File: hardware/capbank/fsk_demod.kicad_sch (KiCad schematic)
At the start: 13 parts, among them U10 TS861IL, U7 4046

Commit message: KiCad changes
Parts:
- removed R16: 10k, PCM_Resistor_SMD_AKL:R_0603_1608Metric, symbol Device:R
- added JP5, JP6: 0, PCM_Resistor_SMD_AKL:R_0603_1608Metric, symbol Jumper:Jumper_2_Small_Open
- C40, C41: value C -> 1n
- R13: value 10k -> 22k
- R14: now not fitted
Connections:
- net at C41.1: now also R15.2, U7.9 (VCOin)
- net at U7.2 (PC1): now also JP6.1 (A); no longer R15.1
- net at U7.13 (PC2): now also JP5.1 (A)
- new net: JP5.2 (B), JP6.2 (B), R15.1
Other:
- moved on the sheet: C41, R15
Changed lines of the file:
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@@
+	)
+	(junction
+		(at 87.63 113.03)
+		(diameter 0)
+		(color 0 0 0 0)
 	)
 	(junction
@@
 	(wire
 		(pts
+			(xy 85.09 115.57) (xy 87.63 115.57)
+		)
+		(stroke
+			(width 0)
+			(type default)
+		)
+	)
+	(wire
+		(pts
 			(xy 52.07 92.71) (xy 52.07 110.49)
 		)
@@
 	(wire
 		(pts
-			(xy 102.87 113.03) (xy 105.41 113.03)
+			(xy 100.33 113.03) (xy 105.41 113.03)
 		)
 		(stroke
@@
 	(wire
 		(pts
-			(xy 80.01 113.03) (xy 95.25 113.03)
-		)
-		(stroke
-			(width 0)
-			(type default)
-		)
-	)
-	(wire
-		(pts
-			(xy 114.3 132.08) (xy 114.3 140.97)
+			(xy 114.3 123.19) (xy 114.3 133.35)
 		)
 		(stroke
@@
 	(wire
 		(pts
+			(xy 87.63 113.03) (xy 87.63 115.57)
+		)
+		(stroke
+			(width 0)
+			(type default)
+		)
+	)
+	(wire
+		(pts
 			(xy 82.55 110.49) (xy 82.55 92.71)
 		)
@@
 	(wire
 		(pts
+			(xy 85.09 113.03) (xy 87.63 113.03)
+		)
+		(stroke
+			(width 0)
+			(type default)
+		)
+	)
+	(wire
+		(pts
 			(xy 105.41 113.03) (xy 105.41 120.65)
 		)
@@
 	(wire
 		(pts
-			(xy 114.3 123.19) (xy 114.3 124.46)
+			(xy 87.63 113.03) (xy 92.71 113.03)
 		)
 		(stroke
@@
 	(symbol
 		(lib_id "Device:C")
-		(at 114.3 128.27 0)
+		(at 114.3 119.38 0)
 		(unit 1)
 		(exclude_from_sim no)
@@
 		(fields_autoplaced yes)
 		(property "Reference" "C41"
-			(at 118.11 126.9999 0)
+			(at 118.11 118.1099 0)
 			(effects
 				(font
@@
 			)
 		)
-		(property "Value" "C"
-			(at 118.11 129.5399 0)
+		(property "Value" "1n"
+			(at 118.11 120.6499 0)
 			(effects
 				(font
@@
 		)
 		(property "Footprint" "PCM_Capacitor_SMD_AKL:C_0603_1608Metric"
-			(at 115.2652 132.08 0)
+			(at 115.2652 123.19 0)
 			(effects
 				(font
@@
 		)
 		(property "Datasheet" "~"
-			(at 114.3 128.27 0)
+			(at 114.3 119.38 0)
 			(effects
 				(font
@@
 		)
 		(property "Description" "Unpolarized capacitor"
-			(at 114.3 128.27 0)
+			(at 114.3 119.38 0)
 			(effects
 				(font
@@
 	)
 	(symbol
-		(lib_id "Device:R")
-		(at 114.3 119.38 0)
-		(unit 1)
-		(exclude_from_sim no)
-		(in_bom yes)
-		(on_board yes)
-		(dnp no)
-		(fields_autoplaced yes)
-		(property "Reference" "R16"
-			(at 116.84 118.1099 0)
-			(effects
-				(font
-					(size 1.27 1.27)
-				)
-				(justify left)
-			)
-		)
-		(property "Value" "10k"
-			(at 116.84 120.6499 0)
-			(effects
-				(font
-					(size 1.27 1.27)
-				)
-				(justify left)
-			)
-		)
-		(property "Footprint" "PCM_Resistor_SMD_AKL:R_0603_1608Metric"
-			(at 112.522 119.38 90)
-			(effects
-				(font
-					(size 1.27 1.27)
-				)
-				(hide yes)
-			)
-		)
-		(property "Datasheet" "~"
-			(at 114.3 119.38 0)
-			(effects
-				(font
-					(size 1.27 1.27)
-				)
-				(hide yes)
-			)
-		)
-		(property "Description" "Resistor"
-			(at 114.3 119.38 0)
-			(effects
-				(font
-					(size 1.27 1.27)
-				)
-				(hide yes)
-			)
-		)
-		(pin "2"
-		)
-		(pin "1"
-		)
-		(instances
-			(project "capbank1"
-				(path "/461cb8a1-2d60-44a8-88b5-d61a3ba14a84/d9c36704-5831-4033-b353-abc8255d1c86/9a2777cd-eff3-4d8b-a149-a95a84199cc5"
-					(reference "R16")
-					(unit 1)
-				)
-			)
-		)
-	)
-	(symbol
 		(lib_id "power:GND")
 		(at 91.44 140.97 0)
@@
 			)
 		)
-		(property "Value" "C"
+		(property "Value" "1n"
 			(at 38.1 120.6499 0)
 			(effects
@@
 			)
 		)
-		(property "Value" "10k"
+		(property "Value" "22k"
 			(at 35.56 137.1599 0)
 			(effects
@@
 		(in_bom yes)
 		(on_board yes)
-		(dnp no)
+		(dnp yes)
 		(fields_autoplaced yes)
 		(property "Reference" "R14"
@@
 	)
 	(symbol
+		(lib_id "Jumper:Jumper_2_Small_Open")
+		(at 82.55 113.03 0)
+		(unit 1)
+		(exclude_from_sim no)
+		(in_bom yes)
+		(on_board yes)
+		(dnp no)
+		(property "Reference" "JP6"
+			(at 85.344 111.252 0)
+			(effects
+				(font
+					(size 1.27 1.27)
+				)
+			)
+		)
+		(property "Value" "0"
+			(at 84.582 109.474 0)
+			(effects
+				(font
+					(size 1.27 1.27)
+				)
+				(hide yes)
+			)
+		)
+		(property "Footprint" "PCM_Resistor_SMD_AKL:R_0603_1608Metric"
+			(at 82.55 113.03 0)
+			(effects
+				(font
+					(size 1.27 1.27)
+				)
+				(hide yes)
+			)
+		)
+		(property "Datasheet" "~"
+			(at 82.55 113.03 0)
+			(effects
+				(font
+					(size 1.27 1.27)
+				)
+				(hide yes)
+			)
+		)
+		(property "Description" "Jumper, 2-pole, small symbol, open"
+			(at 82.55 113.03 0)
+			(effects
+				(font
+					(size 1.27 1.27)
+				)
+				(hide yes)
+			)
+		)
+		(pin "1"
+		)
+		(pin "2"
+		)
+		(instances
+			(project "capbank1"
+				(path "/461cb8a1-2d60-44a8-88b5-d61a3ba14a84/d9c36704-5831-4033-b353-abc8255d1c86/9a2777cd-eff3-4d8b-a149-a95a84199cc5"
+					(reference "JP6")
+					(unit 1)
+				)
+			)
+		)
+	)
+	(symbol
 		(lib_id "Device:C")
 		(at 110.49 96.52 0)
@@
 	(symbol
 		(lib_id "Jumper:Jumper_2_Small_Open")
+		(at 82.55 115.57 0)
+		(unit 1)
+		(exclude_from_sim no)
+		(in_bom yes)
+		(on_board yes)
+		(dnp no)
+		(property "Reference" "JP5"
+			(at 82.55 116.84 0)
+			(effects
+				(font
+					(size 1.27 1.27)
+				)
+			)
+		)
+		(property "Value" "0"
+			(at 82.55 118.618 0)
+			(effects
+				(font
+					(size 1.27 1.27)
+				)
+				(hide yes)
+			)
+		)
+		(property "Footprint" "PCM_Resistor_SMD_AKL:R_0603_1608Metric"
+			(at 82.55 115.57 0)
+			(effects
+				(font
+					(size 1.27 1.27)
+				)
+				(hide yes)
+			)
+		)
+		(property "Datasheet" "~"
+			(at 82.55 115.57 0)
+			(effects
+				(font
+					(size 1.27 1.27)
+				)
+				(hide yes)
+			)
+		)
+		(property "Description" "Jumper, 2-pole, small symbol, open"
+			(at 82.55 115.57 0)
+			(effects
+				(font
+					(size 1.27 1.27)
+				)
+				(hide yes)
+			)
+		)
+		(pin "1"
+		)
+		(pin "2"
+		)
+		(instances
+			(project "capbank1"
+				(path "/461cb8a1-2d60-44a8-88b5-d61a3ba14a84/d9c36704-5831-4033-b353-abc8255d1c86/9a2777cd-eff3-4d8b-a149-a95a84199cc5"
+					(reference "JP5")
+					(unit 1)
+				)
+			)
+		)
+	)
+	(symbol
+		(lib_id "Jumper:Jumper_2_Small_Open")
 		(at 86.36 128.27 0)
 		(unit 1)
@@
 		(on_board yes)
 		(dnp no)
-		(fields_autoplaced yes)
 		(property "Reference" "JP2"
-			(at 86.36 121.92 0)
+			(at 86.36 122.936 0)
 			(effects
 				(font
@@
 		)
 		(property "Value" "0"
-			(at 86.36 124.46 0)
+			(at 86.36 125.476 0)
 			(effects
 				(font
@@
 	(symbol
 		(lib_id "Device:R")
-		(at 99.06 113.03 90)
+		(at 96.52 113.03 90)
 		(unit 1)
 		(exclude_from_sim no)
@@
 		(fields_autoplaced yes)
 		(property "Reference" "R15"
-			(at 99.06 106.68 90)
+			(at 96.52 106.68 90)
 			(effects
 				(font
@@
 		)
 		(property "Value" "10k"
-			(at 99.06 109.22 90)
+			(at 96.52 109.22 90)
 			(effects
 				(font
@@
 		)
 		(property "Footprint" "PCM_Resistor_SMD_AKL:R_0603_1608Metric"
-			(at 99.06 114.808 90)
+			(at 96.52 114.808 90)
 			(effects
 				(font
@@
 		)
 		(property "Datasheet" "~"
-			(at 99.06 113.03 0)
+			(at 96.52 113.03 0)
 			(effects
 				(font
@@
 		)
 		(property "Description" "Resistor"
-			(at 99.06 113.03 0)
+			(at 96.52 113.03 0)
 			(effects
 				(font
@@
 	(symbol
 		(lib_id "power:GND")
-		(at 114.3 140.97 0)
+		(at 114.3 133.35 0)
 		(unit 1)
 		(exclude_from_sim no)
@@
 		(fields_autoplaced yes)
 		(property "Reference" "#PWR0116"
-			(at 114.3 147.32 0)
+			(at 114.3 139.7 0)
 			(effects
 				(font
@@
 		)
 		(property "Value" "GND"
-			(at 114.3 146.05 0)
+			(at 114.3 138.43 0)
 			(effects
 				(font
@@
 		)
 		(property "Footprint" ""
-			(at 114.3 140.97 0)
+			(at 114.3 133.35 0)
 			(effects
 				(font
@@
 		)
 		(property "Datasheet" ""
-			(at 114.3 140.97 0)
+			(at 114.3 133.35 0)
 			(effects
 				(font
@@
 		)
 		(property "Description" "Power symbol creates a global label with name \"GND\" , ground"
-			(at 114.3 140.97 0)
-			(effects
-				(font
+			(at 114.3 133.35 0)
+			(effects
+				(font

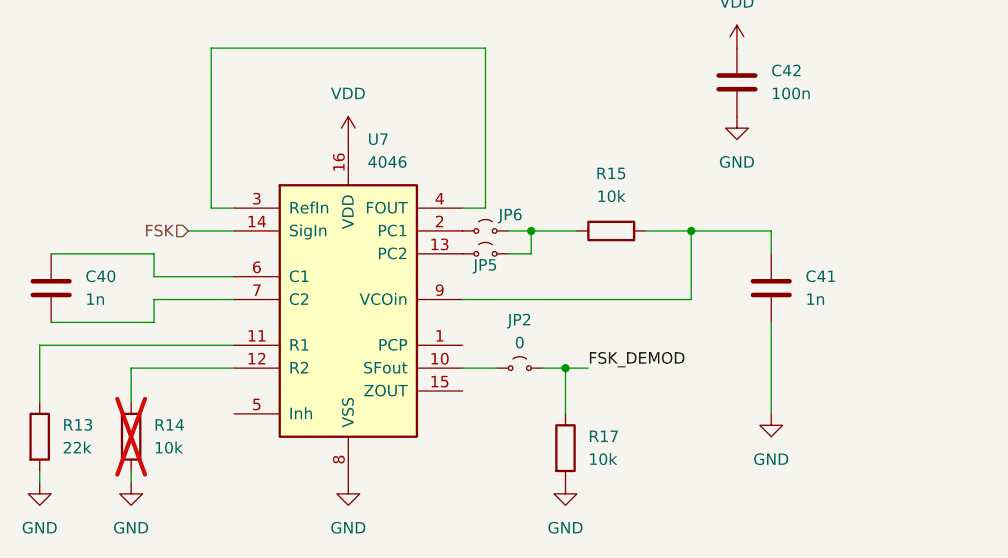
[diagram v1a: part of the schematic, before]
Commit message: Progress, layout nearly completed, build oscillator on breadboard
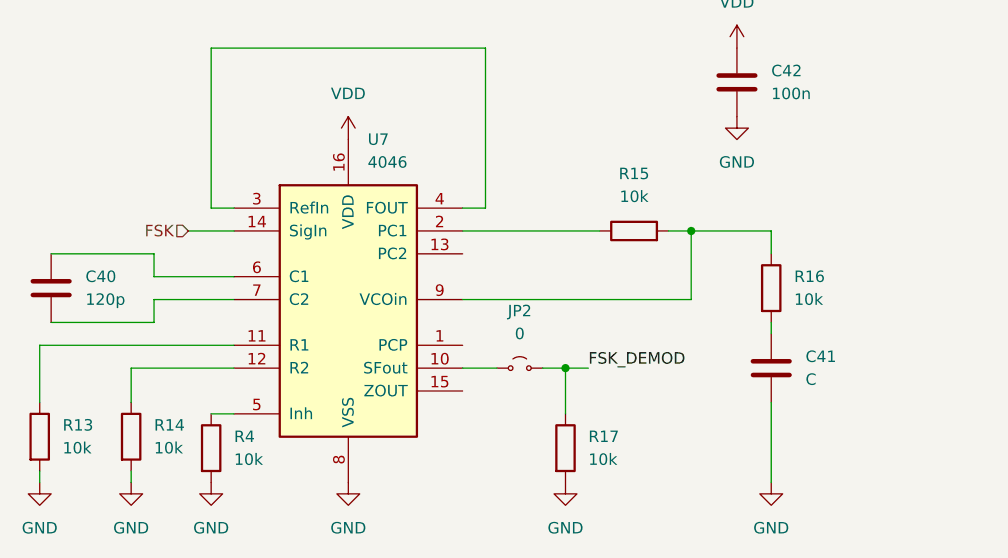
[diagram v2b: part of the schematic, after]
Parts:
- removed JP5, JP6: 0, PCM_Resistor_SMD_AKL:R_0603_1608Metric, symbol Jumper:Jumper_2_Small_Open
- added R16, R4: 10k, PCM_Resistor_SMD_AKL:R_0603_1608Metric, symbol Device:R
- C40: value 1n -> 120p
- C41: value 1n -> C
- R13: value 22k -> 10k
- R14: now fitted
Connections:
- net GND: now also R4.2
- net at R15.2, U7.9 (VCOin): now also R16.1; no longer C41.1
- net at U7.2 (PC1): now also R15.1
- net at U7.5 (Inh): now also R4.1
- new net: C41.1, R16.2
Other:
- moved on the sheet: C41, R15
